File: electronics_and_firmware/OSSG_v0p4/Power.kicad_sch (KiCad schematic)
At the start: 30 parts

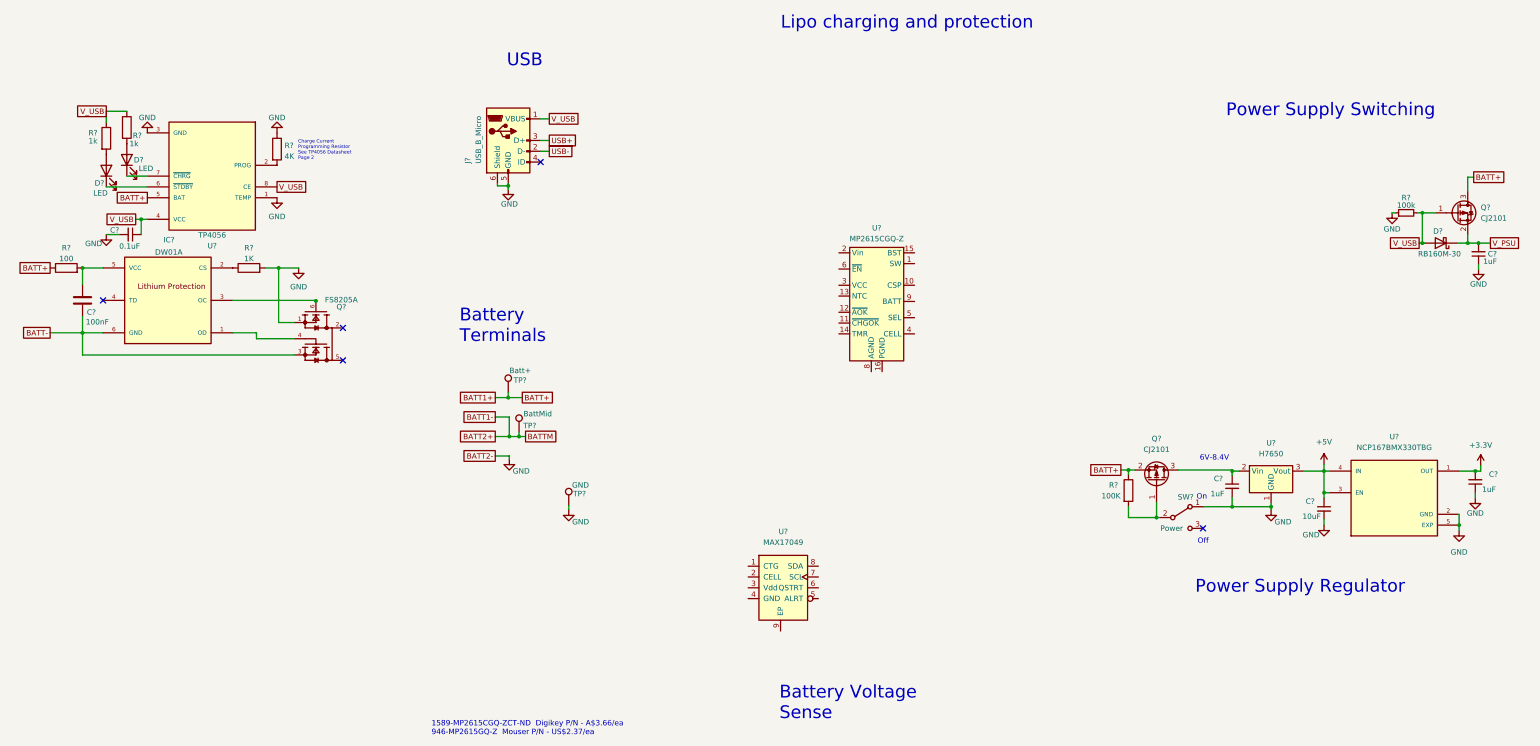
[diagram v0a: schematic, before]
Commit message: filled out MP2615 circuit
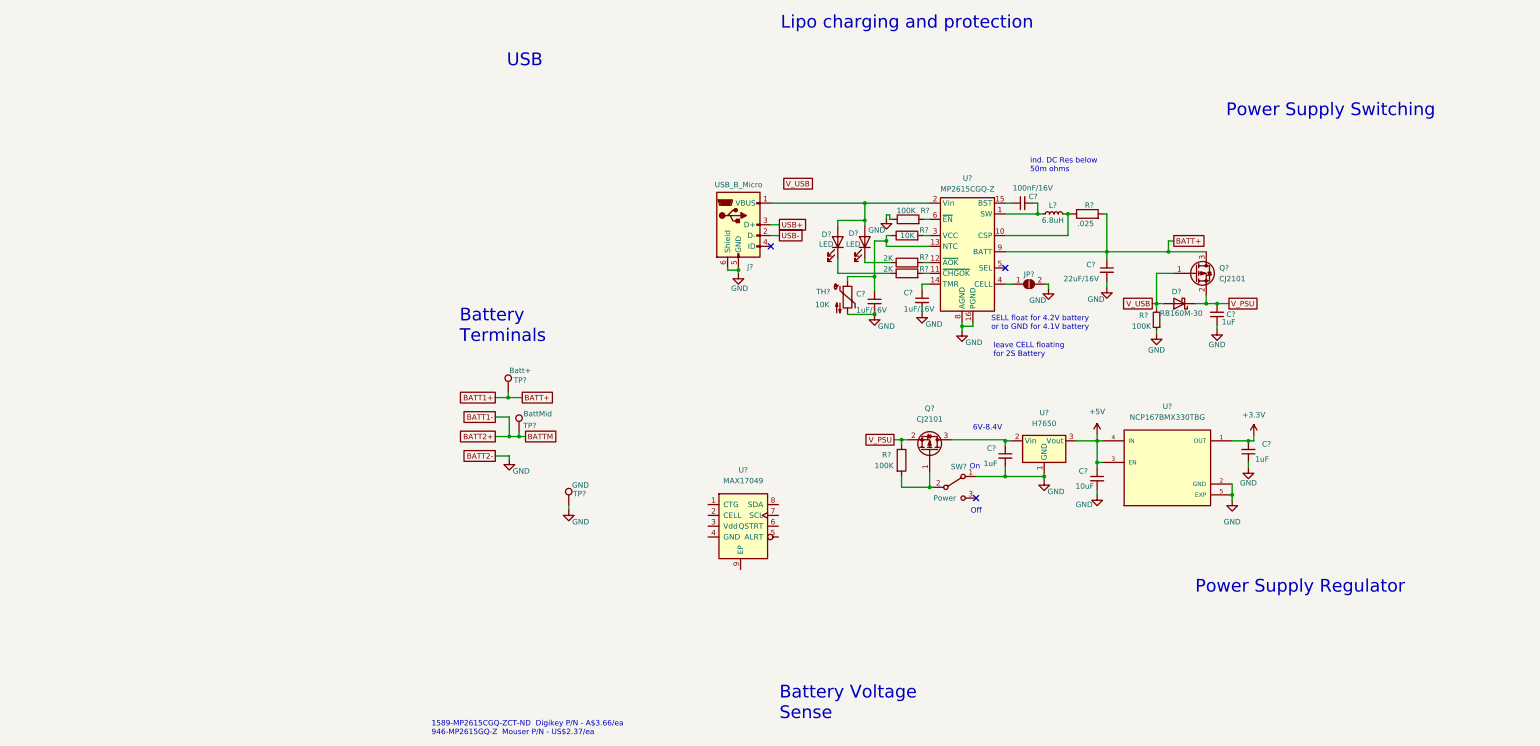
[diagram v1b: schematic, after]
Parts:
- removed C?: 0.1uF, Capacitor_SMD:C_0402_1005Metric, symbol Device:C_Small
- removed C?: 100nF, Capacitor_SMD:C_0402_1005Metric, symbol Device:C
- removed D?: LED, Diode_SMD:D_0402_1005Metric, symbol Device:LED
- removed IC?: DW01A, Package_TO_SOT_SMD:SOT-23-6, symbol DW01A:DW01A
- removed Q?: FS8205A, Package_TO_SOT_SMD:SOT-23-6, symbol FS8205A:FS8205A
- removed R? (x2): 1k, Resistor_SMD:R_0402_1005Metric, symbol Device:R
- removed R?: 4K, Resistor_SMD:R_0402_1005Metric, symbol Device:R
- removed R?: 1K, Resistor_SMD:R_0402_1005Metric, symbol Device:R
- removed R?: 100, Resistor_SMD:R_0402_1005Metric, symbol Device:R
- removed U?: TP4056, Package_SO:SOP-8_5.28x5.23mm_P1.27mm, symbol TP4056:TP4056
- added C? (x2): 1uF/16V, Capacitor_SMD:C_0402_1005Metric, symbol Device:C_Small
- added C?: 100nF/16V, Capacitor_SMD:C_0402_1005Metric, symbol Device:C_Small
- added C?: 22uF/16V, Capacitor_SMD:C_0402_1005Metric, symbol Device:C_Small
- added D?: LED, Diode_SMD:D_0402_1005Metric, symbol Device:LED
- added JP?: SolderJumper_2_Open, OSSG_footprints:JUMPER-2Psml_Open_RoundedPad2x1mm, symbol Jumper:SolderJumper_2_Open
- added L?: 6.8uH, symbol Device:L_Small
- added R? (x2): 2K, Resistor_SMD:R_0402_1005Metric, symbol Device:R
- added R?: 100K, Resistor_SMD:R_0402_1005Metric, symbol Device:R
- added R?: .025, Resistor_SMD:R_0402_1005Metric, symbol Device:R
- added R?: 10K, Resistor_SMD:R_0402_1005Metric, symbol Device:R
- added TH?: 10K, symbol Device:Thermistor_NTC
- R?: value 100k -> 100K
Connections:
- net BATT+: now also U?.9 (BATT), C?.1, R?.2; no longer Q?.2 (S), R?.1
- net GND: now also U?.16 (PGND), U?.8 (AGND), C?.2, C?.2, C?.2, JP?.2 (B), R?.1, TH?.2
- net V_PSU: now also Q?.2 (S), R?.1
- net V_USB: no longer J?.1 (VBUS)
- net at D?.1 (K): now also R?.1
- net at D?.2 (A): now also J?.1 (VBUS), U?.2 (Vin), D?.2 (A)
- net at U?.1 (SW): now also C?.2, L?.1
- net at U?.10 (CSP): now also L?.2, R?.1
- net at U?.11 (~{CHGOK}): now also R?.2
- net at U?.12 (~{AOK}): now also R?.2
- net at U?.13 (NTC): now also C?.1, R?.1, TH?.1
- net at U?.14 (TMR): now also C?.1
- net at U?.15 (BST): now also C?.1
- net at U?.3 (VCC): now also R?.2
- net at U?.4 (CELL): now also JP?.1 (A)
- net at U?.6 (~{EN}): now also R?.2
- new net: D?.1 (K), R?.1
- no-connect marks 5 -> 3
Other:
- note added: "SELL float for 4.2V battery or to GND for 4.1V battery"
- note added: "ind. DC Res below 50m ohms"
- note added: "leave CELL floating for 2S Battery"
- note removed: "Charge Current Programming Resistor See TP4056 Datasheet Page 2"
- moved on the sheet: C?, D?, J?, Q?, R?, SW?, U?

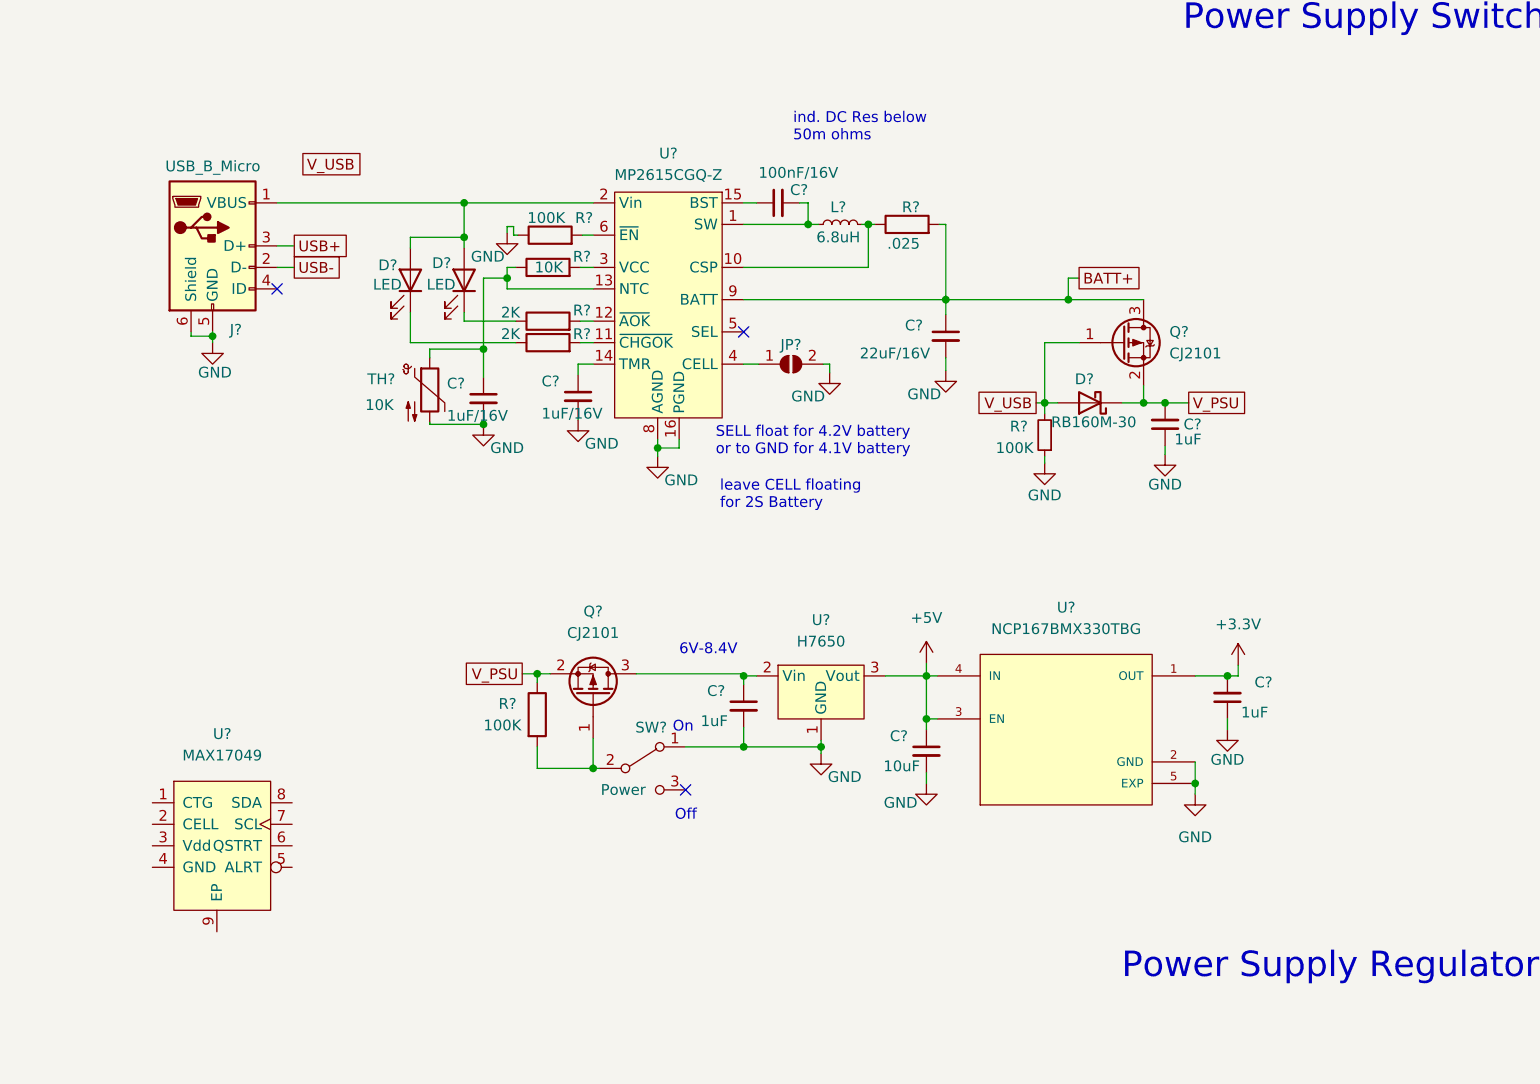
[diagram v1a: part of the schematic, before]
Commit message: about to change power switching MOSFETs
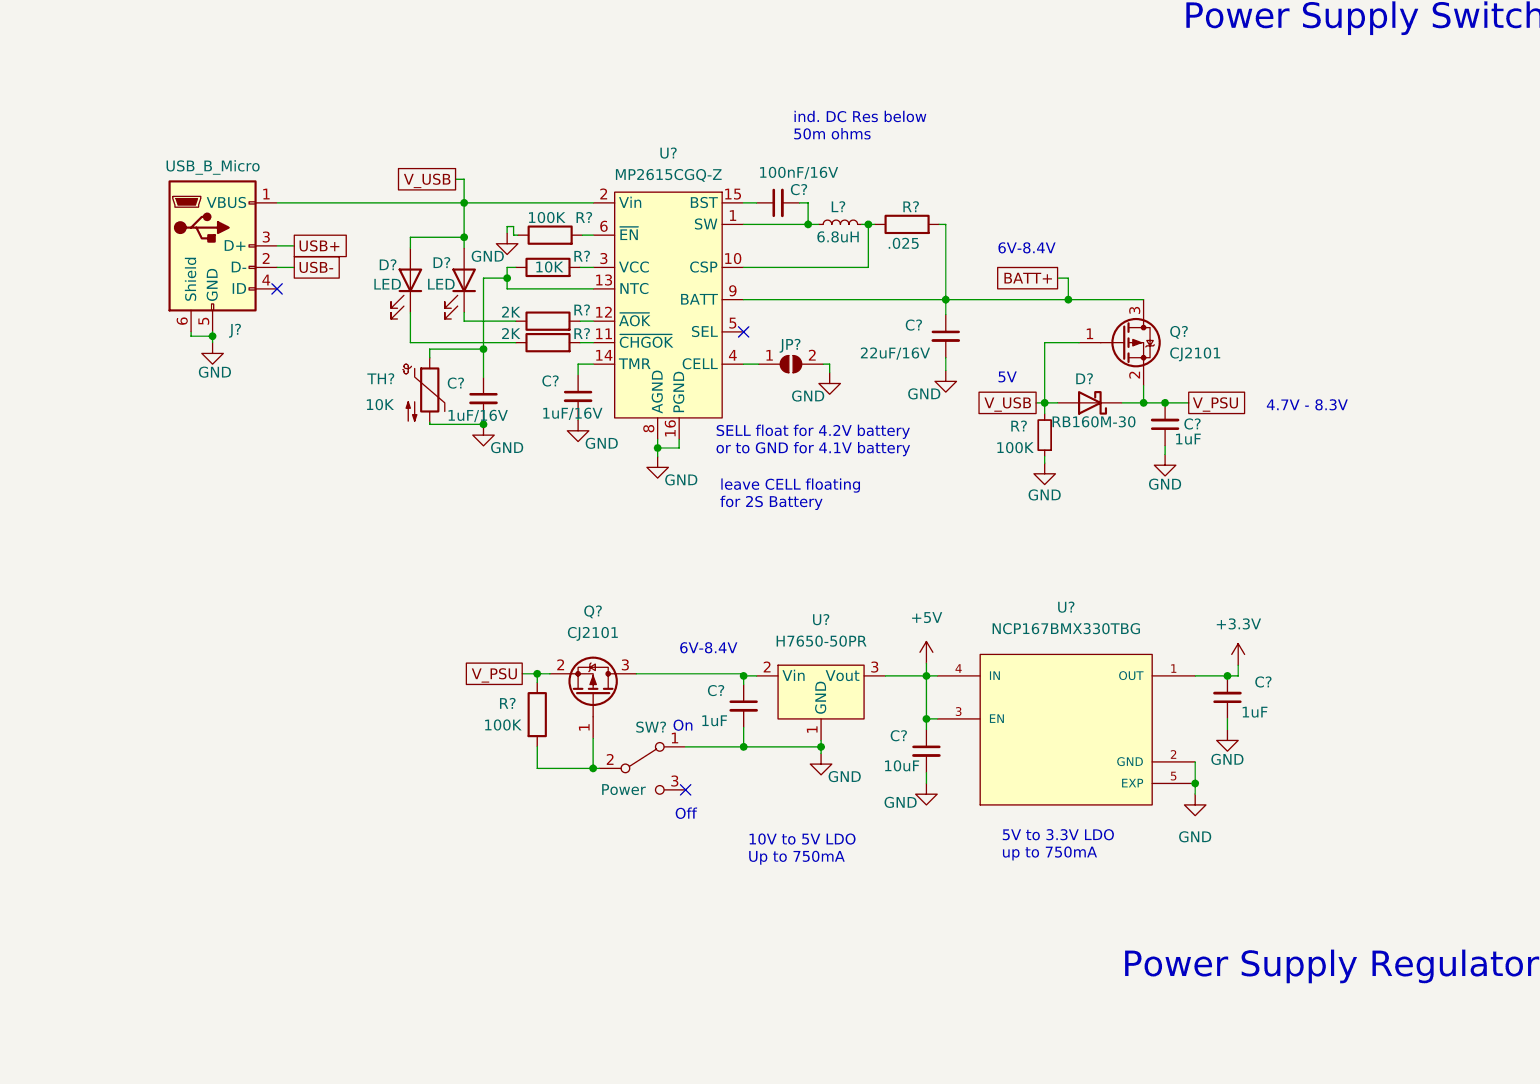
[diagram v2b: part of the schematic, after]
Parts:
- removed U?: MAX17049, symbol OSSG_components_lib:MAX17048
- U?: value H7650 -> H7650-50PR
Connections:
- net V_USB: now also D?.2 (A), D?.2 (A), J?.1 (VBUS), U?.2 (Vin)
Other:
- note added: "10V to 5V LDO Up to 750mA"
- note added: "4.7V - 8.3V"
- note added: "5V"
- note added: "5V to 3.3V LDO up to 750mA"
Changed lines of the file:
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@@
+    (stroke (width 0) (type default) (color 0 0 0 0))
+  )
+  (wire (pts (xy 126.746 66.04) (xy 126.746 68.834))
     (stroke (width 0) (type default) (color 0 0 0 0))
   )
@@
     (stroke (width 0) (type default) (color 0 0 0 0))
   )
+  (wire (pts (xy 125.73 66.04) (xy 126.746 66.04))
+    (stroke (width 0) (type default) (color 0 0 0 0))
+  )
   (wire (pts (xy 104.648 76.454) (xy 106.68 76.454))
     (stroke (width 0) (type default) (color 0 0 0 0))
@@
     (stroke (width 0) (type default) (color 0 0 0 0))
   )
-  (wire (pts (xy 199.39 77.724) (xy 198.12 77.724))
+  (wire (pts (xy 196.85 77.724) (xy 198.12 77.724))
     (stroke (width 0) (type default) (color 0 0 0 0))
   )
@@
     (effects (font (size 3 3)) (justify right bottom))
   )
+  (text "10V to 5V LDO\nUp to 750mA" (at 160.274 147.066 0)
+    (effects (font (size 1.27 1.27)) (justify left bottom))
+  )
+  (text "6V-8.4V" (at 189.738 75.184 0)
+    (effects (font (size 1.27 1.27)) (justify left bottom))
+  )
   (text "6V-8.4V" (at 152.146 122.428 0)
     (effects (font (size 1.27 1.27)) (justify left bottom))
   )
+  (text "5V to 3.3V LDO\nup to 750mA" (at 190.246 146.558 0)
+    (effects (font (size 1.27 1.27)) (justify left bottom))
+  )
   (text "Off" (at 151.638 141.986 0)
     (effects (font (size 1.27 1.27)) (justify left bottom))
   )
+  (text "5V" (at 189.738 90.424 0)
+    (effects (font (size 1.27 1.27)) (justify left bottom))
+  )
   (text "ind. DC Res below \n50m ohms" (at 165.608 61.722 0)
     (effects (font (size 1.27 1.27)) (justify left bottom))
@@
   (text "1589-MP2615CGQ-ZCT-ND  Digikey P/N - A$3.66/ea\n946-MP2615GQ-Z  Mouser P/N - US$2.37/ea"
     (at 24.892 194.056 0)
+    (effects (font (size 1.27 1.27)) (justify left bottom))
+  )
+  (text "4.7V - 8.3V" (at 221.488 93.726 0)
     (effects (font (size 1.27 1.27)) (justify left bottom))
   )
@@
     )
   )
-  (global_label "V_USB" (shape passive) (at 107.696 64.262 0) (fields_autoplaced)
-    (effects (font (size 1.27 1.27)) (justify left))
-    (property "Intersheet References" "${INTERSHEET_REFS}" (id 0) (at 115.9753 64.3414 0)
-      (effects (font (size 1.27 1.27)) (justify left) hide)
+  (global_label "V_USB" (shape passive) (at 125.73 66.04 180) (fields_autoplaced)
+    (effects (font (size 1.27 1.27)) (justify right))
+    (property "Intersheet References" "${INTERSHEET_REFS}" (id 0) (at 117.4507 65.9606 0)
+      (effects (font (size 1.27 1.27)) (justify right) hide)
     )
   )
@@
     )
   )
-  (global_label "BATT+" (shape passive) (at 199.39 77.724 0) (fields_autoplaced)
-    (effects (font (size 1.27 1.27)) (justify left))
-    (property "Intersheet References" "${INTERSHEET_REFS}" (id 0) (at 207.6693 77.8034 0)
-      (effects (font (size 1.27 1.27)) (justify left) hide)
+  (global_label "BATT+" (shape passive) (at 196.85 77.724 180) (fields_autoplaced)
+    (effects (font (size 1.27 1.27)) (justify right))
+    (property "Intersheet References" "${INTERSHEET_REFS}" (id 0) (at 188.5707 77.6446 0)
+      (effects (font (size 1.27 1.27)) (justify right) hide)
     )
   )
@@
     (in_bom yes) (on_board yes) (fields_autoplaced)
     (property "Reference" "U?" (id 0) (at 168.91 118.11 0))
-    (property "Value" "H7650" (id 1) (at 168.91 120.65 0))
+    (property "Value" "H7650-50PR" (id 1) (at 168.91 120.65 0))
     (property "Footprint" "Package_TO_SOT_SMD:SOT-89-3" (id 2) (at 173.99 137.414 0)
       (effects (font (size 1.27 1.27)) hide)
@@
     (pin "2")
   )
-  (symbol (lib_id "OSSG_components_lib:MAX17048") (at 97.536 143.51 0) (unit 1)
-    (in_bom yes) (on_board yes) (fields_autoplaced)
-    (property "Reference" "U?" (id 0) (at 98.171 131.572 0))
-    (property "Value" "MAX17049" (id 1) (at 98.171 134.112 0))
-    (property "Footprint" "" (id 2) (at 97.536 143.51 0)
-      (effects (font (size 1.27 1.27)) hide)
-    )
-    (property "Datasheet" "" (id 3) (at 97.536 143.51 0)
-      (effects (font (size 1.27 1.27)) hide)
-    )
-    (pin "1")
-    (pin "2")
-    (pin "3")
-    (pin "4")
-    (pin "5")
-    (pin "6")
-    (pin "7")
-    (pin "8")
-    (pin "9")
-  )
   (symbol (lib_id "Device:C_Small") (at 129.032 91.948 0) (unit 1)

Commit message: V0.4.1 schematic
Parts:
- removed Q? (x2): CJ2101, Package_TO_SOT_SMD:SOT-323_SC-70, symbol OSSG_components_lib:CJ2101
- removed R?: 100K, Resistor_SMD:R_0402_1005Metric, symbol Device:R
- added C12: 100nF, Capacitor_SMD:C_0402_1005Metric, symbol Device:C_Small
- added Q3: PMZ290UNE2YL, OSSG_footprints:DFN100X60X40-3N, symbol OSSG_components_lib:PMZ290UNE2YL
- added Q4: EMF20B02V, Package_TO_SOT_SMD:SOT-23-6, symbol OSSG_components_lib:EMF20B02V
- added R15, R19: 884K, Resistor_SMD:R_0402_1005Metric, symbol Device:R_Small
- added R16: 320K, Resistor_SMD:R_0402_1005Metric, symbol Device:R_Small
- added R18: 100K, Resistor_SMD:R_0402_1005Metric, symbol Device:R_Small
- added R6: 100k, Resistor_SMD:R_0402_1005Metric, symbol Device:R_Small
- added U4: XC61CC3002MR, Package_TO_SOT_SMD:SOT-23, symbol OSSG_components_lib:XC61C_voltage_supervisor
- SW2: renamed from SW?; footprint (none) -> OSSG_footprints:SW_SMD_SPDT_Slide_9x6.9-hole
- TH1: renamed from TH?; footprint (none) -> Connector_PinHeader_1.27mm:PinHeader_1x02_P1.27mm_Horizontal
- U5: renamed from U?; footprint (none) -> OSSG_footprints:MP2615GQ-P
- gave numbers to parts that had none: 25
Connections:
- net BATT+: now also Q4.1 (S2), R15.1, R19.2
- net BATT1-: now also C12.1, R6.1, U4.3 (VIN)
- net GND: now also C12.2, Q3.2 (S), R16.2, R18.1, U4.2 (GND/VSS)
- net V_PSU: now also C17.1, U6.2 (Vin), Q4.3 (S2)
- net V_USB: now also Q4.4 (G2)
- net PSEN: now reaches SW2.2 (B)
- net PSEN: now also Q3.1 (G), R18.2, R6.2, U4.1 (VOUT)
- new net: Q3.3 (D), Q4.2 (G2), R19.1
- new net: Q4.5 (D2), Q4.7 (D2)
- new net: Q4.6 (D2), Q4.8 (D2)
- new net IO36: R15.2, R16.1
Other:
- note added: "* Note: need to test how well the H7650 LDO passes the USB 4.6V thru to the otherside"
- note added: "4.6V - 8.2V"
- note added: "Voltage Supervisor"
- note added: "will be supplying 50mA to GND while switched on"
- note removed: "4.7V - 8.3V"
- note removed: "5V"
- moved on the sheet: C13, C14, C15, C16, C17, C18, C19, C20, D5, D6, D7, J2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
